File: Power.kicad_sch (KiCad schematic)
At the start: 30 parts, among them J6 USB_C_USB2.0_16P, Q1 Si2301CDS, SW3 CHRG_EN, U3 TP4056, U4 AMS1117-3.3, U5 TPS61230DRCR

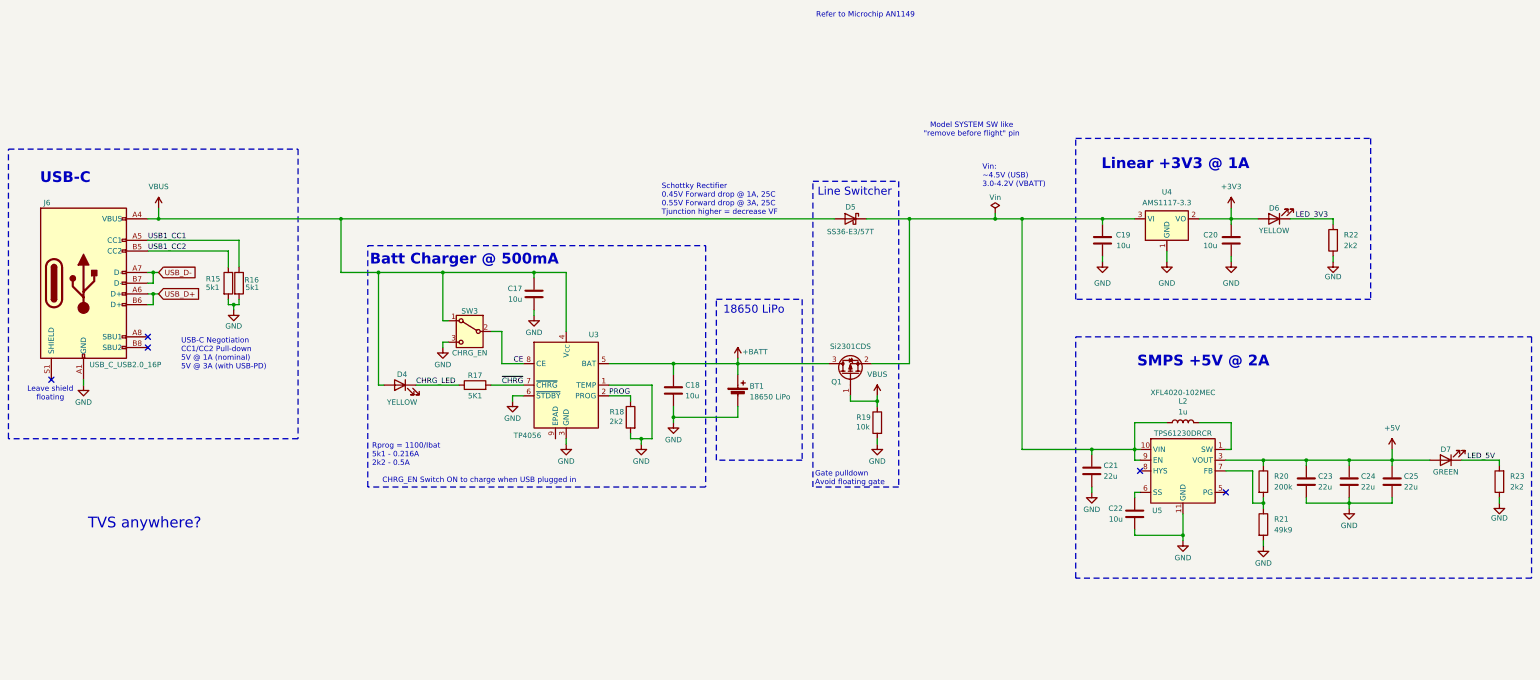
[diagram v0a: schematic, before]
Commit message: Added footprints & routing 30%
- Added Dupont debug headers for UARTs.
- Added footprints: 18650 battery, E32-400M30S.
- Remove Battery Charger due to reliability issue.
- Routing 5V SMPS, 3V3 Regulator, Battery Holder.
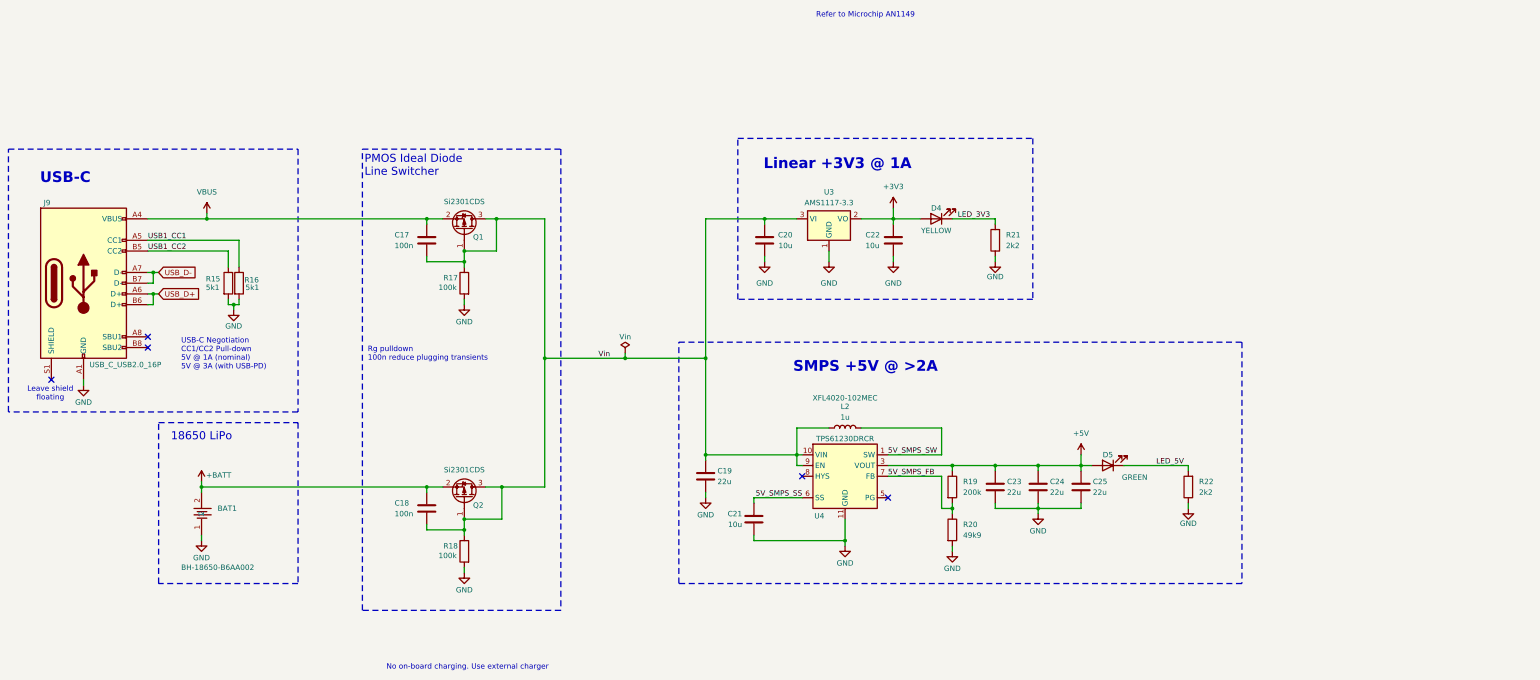
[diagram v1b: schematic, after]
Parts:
- removed BT1: 18650 LiPo, parallel18650:18650-PC4, symbol Device:Battery_Cell
- removed D4: YELLOW, LED_SMD:LED_0805_2012Metric, symbol Device:LED
- removed D5: SS36-E3/57T, Diode_SMD:D_SMC, symbol Diode:MBRS340
- removed R18: 2k2, Resistor_SMD:R_0402_1005Metric, symbol Device:R
- removed SW3: CHRG_EN, symbol Switch:SW_SPDT
- removed U3: TP4056, Package_SO:SOIC-8-1EP_3.9x4.9mm_P1.27mm_EP2.41x3.3mm_ThermalVias, symbol Battery_Management:TP4056-42-ESOP8
- added BAT1: BH-18650-B6AA002, easyeda2kicad:BATTERY-SMD_18650-1S-L77.1-W20.7-1, symbol easyeda2kicad:BH-18650-B6AA002
- added Q1: Si2301CDS, Package_TO_SOT_SMD:SOT-23, symbol Transistor_FET:DMG2301L
- C17, C18: value 10u -> 100n; footprint Capacitor_SMD:C_0603_1608Metric -> Capacitor_SMD:C_0402_1005Metric
- C20: renamed from C19; footprint Capacitor_SMD:C_0402_1005Metric -> Capacitor_SMD:C_0805_2012Metric
- C21: renamed from C22; footprint Capacitor_SMD:C_0805_2012Metric -> Capacitor_SMD:C_0603_1608Metric
- C22: renamed from C20; footprint Capacitor_SMD:C_0402_1005Metric -> Capacitor_SMD:C_0805_2012Metric
- R17: value 5K1 -> 100k
- R18: renamed from R19; value 10k -> 100k; footprint Resistor_SMD:R_0603_1608Metric -> Resistor_SMD:R_0402_1005Metric
- renumbered C21 to C19, D6 to D4, D7 to D5, J6 to J9, Q1 to Q2, R20 to R19, R21 to R20, R22 to R21, R23 to R22, U4 to U3, U5 to U4
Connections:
- net CHRG_LED is gone; now on net Vin: R17.1
- net ~{CHRG} is gone; now on net GND: R17.2
- net +BATT: now also Q2.2 (S), BAT1.2; no longer Q2.3 (D)
- net GND: now also BAT1.1; no longer C17.2, C18.2
- net VBUS: now also Q1.2 (S); no longer Q2.1 (G), R18.1
- net Vin: now reaches C19.1, C20.1, L2.1, U3.3 (VI), U4.10 (VIN), U4.9 (EN)
- net Vin: now also C17.2, C18.2, Q2.1 (G), Q2.3 (D), R18.1, Q1.1 (G), Q1.3 (D); no longer Q2.2 (S)
- net 5V_SMPS_FB: now reaches R19.2, R20.1, U4.7 (FB)
- net 5V_SMPS_SW: now reaches L2.2, U4.1 (SW), U4.2 (SW)
- net 5V_SMPS_SS: now reaches C21.1, U4.6 (SS)
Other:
- note added: "No on-board charging. Use external charger"
- note added: "PMOS Ideal Diode Line Switcher"
- note added: "Rg pulldown 100n reduce plugging transients"
- note added: "SMPS +5V @ >2A"
- note removed: "Batt Charger @ 500mA"
- note removed: "CHRG_EN Switch ON to charge when USB plugged in"
- note removed: "Gate pulldown Avoid floating gate"
- note removed: "Line Switcher"
- note removed: "Model SYSTEM SW like "remove before flight" pin"
- note removed: "Rprog = 1100/Ibat 5k1 - 0.216A 2k2 - 0.5A"
- note removed: "SMPS +5V @ 2A"
- note removed: "Schottky Rectifier 0.45V Forward drop @ 1A, 25C 0.55V Forward drop @ 3A, 25C Tjunction higher = decrease VF"
- note removed: "TVS anywhere?"
- note removed: "Vin: ~4.5V (USB) 3.0-4.2V (VBATT)"
- moved on the sheet: C19, C20, C21, C22, C23, C24, C25, D4, D5, L2, Q2, R18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

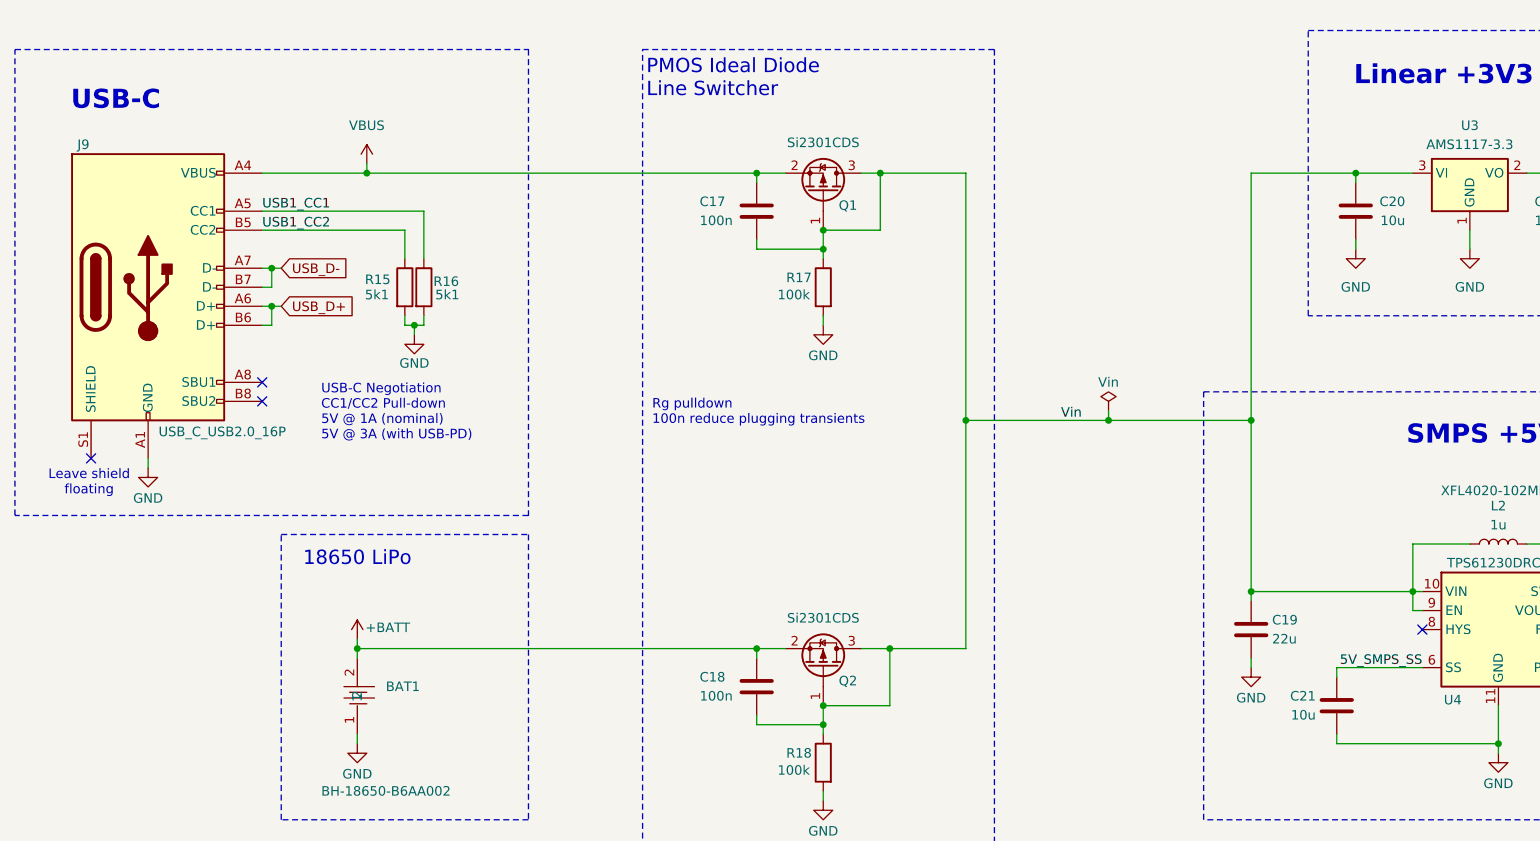
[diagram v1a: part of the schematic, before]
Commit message: Finished layout & DRC
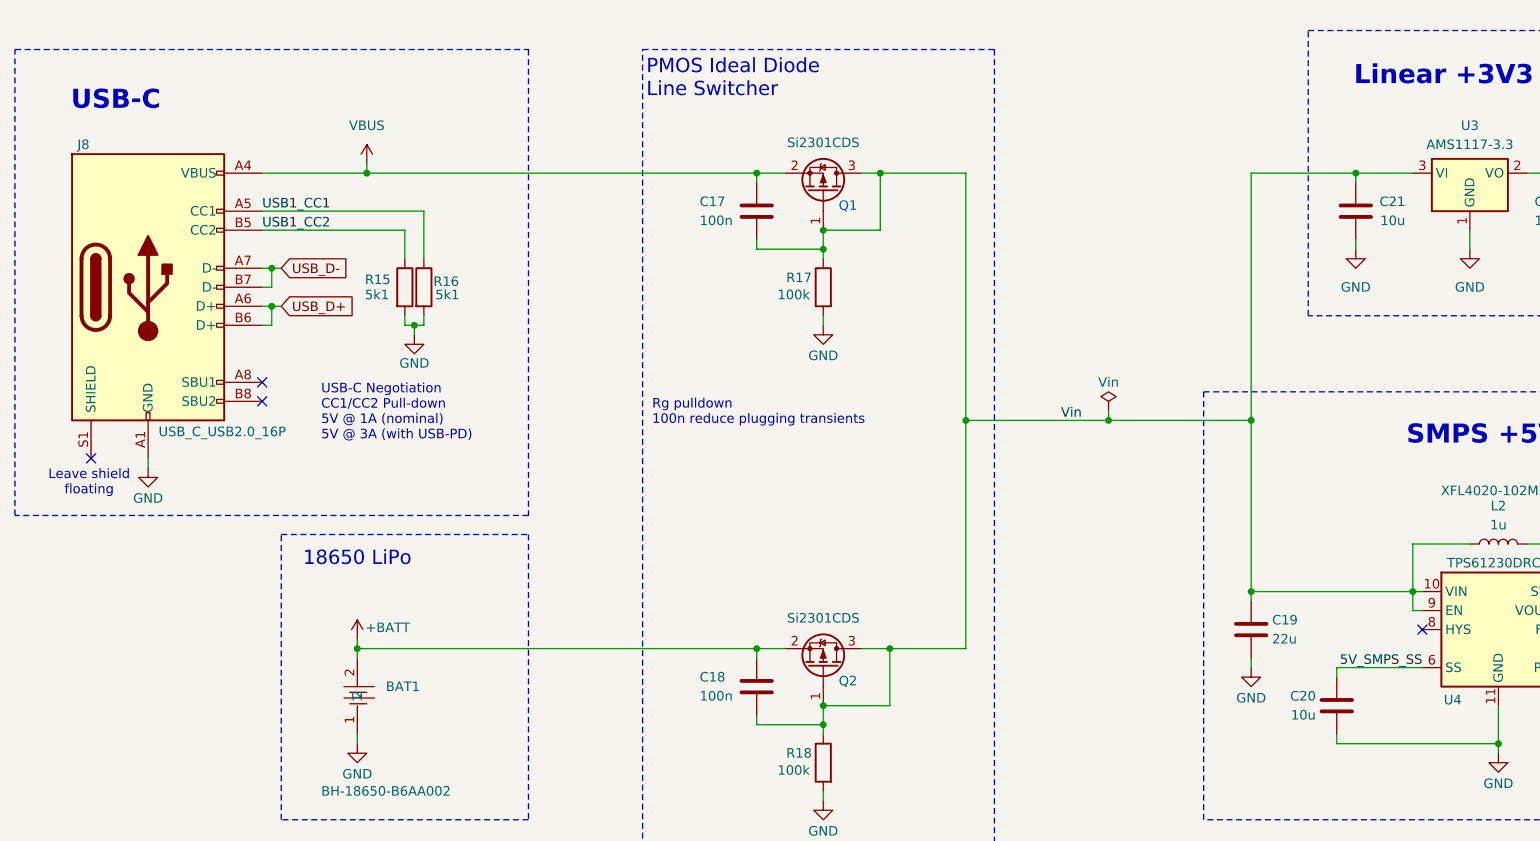
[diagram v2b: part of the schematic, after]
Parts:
- J8: renamed from J9; footprint Connector_USB:USB_C_Receptacle_Molex_105450-0101 -> Connector_USB:USB_C_Receptacle_HRO_TYPE-C-31-M-12
- renumbered C21 to C20, C20 to C21
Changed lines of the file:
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@@
 		(dnp no)
 		(fields_autoplaced yes)
-		(property "Reference" "#PWR047"
+		(property "Reference" "#PWR044"
 			(at 287.02 123.19 0)
 			(effects
@@
 			(project ""
 				(path "/e98ed281-6a46-49b2-ab41-e3d95fdf6973/2ac26712-adbd-4e92-84f1-3c660d93b184"
-					(reference "#PWR047")
+					(reference "#PWR044")
 					(unit 1)
 				)
@@
 		(on_board yes)
 		(dnp no)
-		(property "Reference" "C20"
+		(property "Reference" "C21"
 			(at 218.694 67.31 0)
 			(effects
@@
 			(project "BLV_PCB"
 				(path "/e98ed281-6a46-49b2-ab41-e3d95fdf6973/2ac26712-adbd-4e92-84f1-3c660d93b184"
-					(reference "C20")
+					(reference "C21")
 					(unit 1)
 				)
@@
 		(on_board yes)
 		(dnp no)
-		(property "Reference" "#PWR041"
+		(property "Reference" "#PWR038"
 			(at 231.14 147.32 0)
 			(effects
@@
 			(project "BLV_PCB"
 				(path "/e98ed281-6a46-49b2-ab41-e3d95fdf6973/2ac26712-adbd-4e92-84f1-3c660d93b184"
-					(reference "#PWR041")
+					(reference "#PWR038")
 					(unit 1)
 				)
@@
 		(dnp no)
 		(fields_autoplaced yes)
-		(property "Reference" "#PWR040"
+		(property "Reference" "#PWR037"
 			(at 227.33 80.01 0)
 			(effects
@@
 			(project "BLV_PCB"
 				(path "/e98ed281-6a46-49b2-ab41-e3d95fdf6973/2ac26712-adbd-4e92-84f1-3c660d93b184"
-					(reference "#PWR040")
+					(reference "#PWR037")
 					(unit 1)
 				)
@@
 		(on_board yes)
 		(dnp no)
-		(property "Reference" "#PWR046"
+		(property "Reference" "#PWR043"
 			(at 276.86 139.7 0)
 			(effects
@@
 			(project "BLV_PCB"
 				(path "/e98ed281-6a46-49b2-ab41-e3d95fdf6973/2ac26712-adbd-4e92-84f1-3c660d93b184"
-					(reference "#PWR046")
+					(reference "#PWR043")
 					(unit 1)
 				)
@@
 		(dnp no)
 		(fields_autoplaced yes)
-		(property "Reference" "#PWR042"
+		(property "Reference" "#PWR039"
 			(at 242.57 64.77 0)
 			(effects
@@
 			(project "BLV_PCB"
 				(path "/e98ed281-6a46-49b2-ab41-e3d95fdf6973/2ac26712-adbd-4e92-84f1-3c660d93b184"
-					(reference "#PWR042")
+					(reference "#PWR039")
 					(unit 1)
 				)
@@
 		(dnp no)
 		(fields_autoplaced yes)
-		(property "Reference" "#PWR043"
+		(property "Reference" "#PWR040"
 			(at 242.57 80.01 0)
 			(effects
@@
 			(project "BLV_PCB"
 				(path "/e98ed281-6a46-49b2-ab41-e3d95fdf6973/2ac26712-adbd-4e92-84f1-3c660d93b184"
-					(reference "#PWR043")
+					(reference "#PWR040")
 					(unit 1)
 				)
@@
 		(on_board yes)
 		(dnp no)
-		(property "Reference" "#PWR031"
+		(property "Reference" "#PWR028"
 			(at 50.8 109.22 0)
 			(effects
@@
 			(project "BLV_PCB"
 				(path "/e98ed281-6a46-49b2-ab41-e3d95fdf6973/2ac26712-adbd-4e92-84f1-3c660d93b184"
-					(reference "#PWR031")
+					(reference "#PWR028")
 					(unit 1)
 				)
@@
 		(on_board yes)
 		(dnp no)
-		(property "Reference" "#PWR035"
+		(property "Reference" "#PWR032"
 			(at 86.36 91.44 0)
 			(effects
@@
 			(project "BLV_PCB"
 				(path "/e98ed281-6a46-49b2-ab41-e3d95fdf6973/2ac26712-adbd-4e92-84f1-3c660d93b184"
-					(reference "#PWR035")
+					(reference "#PWR032")
 					(unit 1)
 				)
@@
 		(on_board yes)
 		(dnp no)
-		(property "Reference" "#PWR033"
+		(property "Reference" "#PWR030"
 			(at 78.74 146.05 0)
 			(effects
@@
 			(project "BLV_PCB"
 				(path "/e98ed281-6a46-49b2-ab41-e3d95fdf6973/2ac26712-adbd-4e92-84f1-3c660d93b184"
-					(reference "#PWR033")
+					(reference "#PWR030")
 					(unit 1)
 				)
@@
 		(dnp no)
 		(fields_autoplaced yes)
-		(property "Reference" "#PWR039"
+		(property "Reference" "#PWR036"
 			(at 212.09 80.01 0)
 			(effects
@@
 			(project "BLV_PCB"
 				(path "/e98ed281-6a46-49b2-ab41-e3d95fdf6973/2ac26712-adbd-4e92-84f1-3c660d93b184"
-					(reference "#PWR039")
+					(reference "#PWR036")
 					(unit 1)
 				)
@@
 		(on_board yes)
 		(dnp no)
-		(property "Reference" "#PWR038"
+		(property "Reference" "#PWR035"
 			(at 198.12 135.89 0)
 			(effects
@@
 			(project "BLV_PCB"
 				(path "/e98ed281-6a46-49b2-ab41-e3d95fdf6973/2ac26712-adbd-4e92-84f1-3c660d93b184"
-					(reference "#PWR038")
+					(reference "#PWR035")
 					(unit 1)
 				)
@@
 		(on_board yes)
 		(dnp no)
-		(property "Reference" "#PWR048"
+		(property "Reference" "#PWR045"
 			(at 312.42 138.43 0)
 			(effects
@@
 			(project "BLV_PCB"
 				(path "/e98ed281-6a46-49b2-ab41-e3d95fdf6973/2ac26712-adbd-4e92-84f1-3c660d93b184"
-					(reference "#PWR048")
+					(reference "#PWR045")
 					(unit 1)
 				)
@@
 		(on_board yes)
 		(dnp no)
-		(property "Reference" "#PWR045"
+		(property "Reference" "#PWR042"
 			(at 266.7 80.01 0)
 			(effects
@@
 			(project "BLV_PCB"
 				(path "/e98ed281-6a46-49b2-ab41-e3d95fdf6973/2ac26712-adbd-4e92-84f1-3c660d93b184"
-					(reference "#PWR045")
+					(reference "#PWR042")
 					(unit 1)
 				)
@@
 		(on_board yes)
 		(dnp no)
-		(property "Reference" "#PWR044"
+		(property "Reference" "#PWR041"
 			(at 256.54 148.59 0)
 			(effects
@@
 			(project "BLV_PCB"
 				(path "/e98ed281-6a46-49b2-ab41-e3d95fdf6973/2ac26712-adbd-4e92-84f1-3c660d93b184"
-					(reference "#PWR044")
+					(reference "#PWR041")
 					(unit 1)
 				)
@@
 		(on_board yes)
 		(dnp no)
-		(property "Reference" "J9"
+		(property "Reference" "J8"
 			(at 42.164 59.69 0)
 			(effects
@@
 			)
 		)
-		(property "Footprint" "Connector_USB:USB_C_Receptacle_Molex_105450-0101"
+		(property "Footprint" "Connector_USB:USB_C_Receptacle_HRO_TYPE-C-31-M-12"
 			(at 54.61 78.74 0)
 			(effects
@@
 			(project "BLV_PCB"
 				(path "/e98ed281-6a46-49b2-ab41-e3d95fdf6973/2ac26712-adbd-4e92-84f1-3c660d93b184"
-					(reference "J9")
+					(reference "J8")
 					(unit 1)
 				)
@@
 		(on_board yes)
 		(dnp no)
-		(property "Reference" "#PWR036"
+		(property "Reference" "#PWR033"
 			(at 140.97 90.17 0)
 			(effects
@@
 			(project "BLV_PCB"
 				(path "/e98ed281-6a46-49b2-ab41-e3d95fdf6973/2ac26712-adbd-4e92-84f1-3c660d93b184"
-					(reference "#PWR036")
+					(reference "#PWR033")
 					(unit 1)
 				)
@@
 		(on_board yes)
 		(dnp no)
-		(property "Reference" "C21"
+		(property "Reference" "C20"
 			(at 206.756 133.35 0)
 			(effects
@@
 			(project "BLV_PCB"
 				(path "/e98ed281-6a46-49b2-ab41-e3d95fdf6973/2ac26712-adbd-4e92-84f1-3c660d93b184"
-					(reference "C21")
+					(reference "C20")
 					(unit 1)
 				)
@@
 		(on_board yes)
 		(dnp no)
-		(property "Reference" "#PWR037"
+		(property "Reference" "#PWR034"
 			(at 140.97 153.67 0)
 			(effects
@@
 			(project "BLV_PCB"
 				(path "/e98ed281-6a46-49b2-ab41-e3d95fdf6973/2ac26712-adbd-4e92-84f1-3c660d93b184"
-					(reference "#PWR037")
+					(reference "#PWR034")
 					(unit 1)
 				)
@@
 		(dnp no)
 		(fields_autoplaced yes)
-		(property "Reference" "#PWR034"
+		(property "Reference" "#PWR031"
 			(at 80.01 66.04 0)
 			(effects
@@
 			(project ""
 				(path "/e98ed281-6a46-49b2-ab41-e3d95fdf6973/2ac26712-adbd-4e92-84f1-3c660d93b184"
-					(reference "#PWR034")
+					(reference "#PWR031")
 					(unit 1)
 				)
@@
 		(on_board yes)
 		(dnp no)
-		(property "Reference" "#PWR032"
+		(property "Reference" "#PWR029"
 			(at 78.74 129.54 0)
 			(effects
@@
 			(project "BLV_PCB"
 				(path "/e98ed281-6a46-49b2-ab41-e3d95fdf6973/2ac26712-adbd-4e92-84f1-3c660d93b184"
-					(reference "#PWR032")
-					(unit 1)
-				)
+					(reference "#PWR029")
+					(unit 1)
+				)
